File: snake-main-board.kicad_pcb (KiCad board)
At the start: 2 copper layers, 2 parts

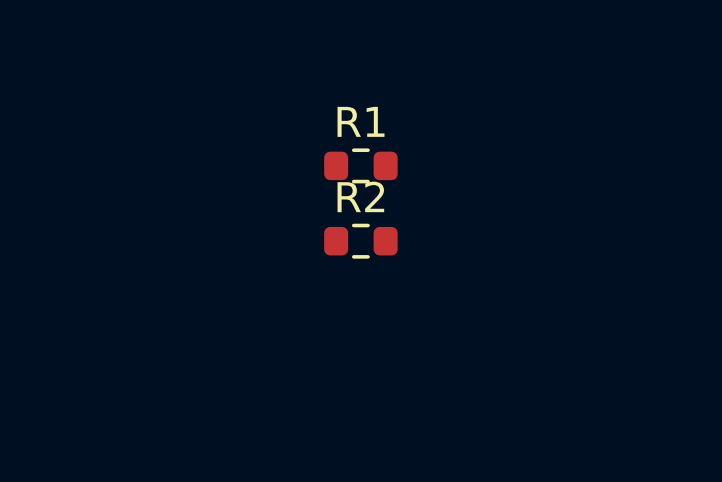
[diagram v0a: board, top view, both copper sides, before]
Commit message: PCB: board outline (20x12 mm), R2 placed 5 mm below R1, two 0.25 mm tracks matching the schematic nets (pcbnew; DRC 0 errors, 0 unconnected, 0 parity issues)
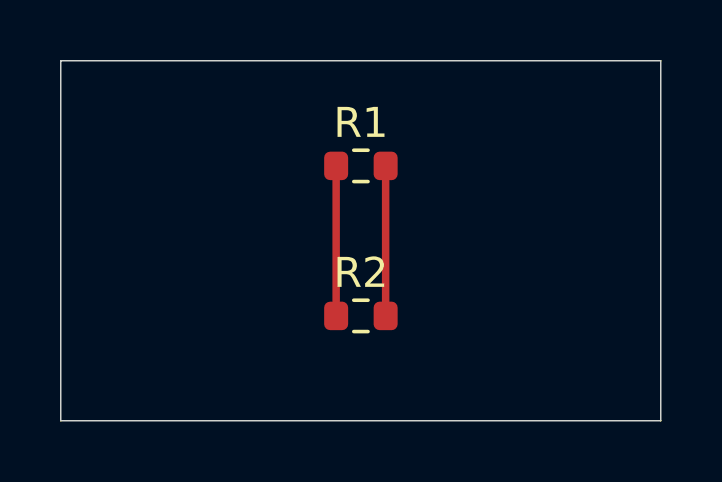
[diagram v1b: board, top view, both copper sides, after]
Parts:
- moved R2 2.49 mm to (129.5, 97.3)
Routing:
- net Net-(R1-Pad2): track 0.00 -> 5.00 mm
- net Net-(R1-Pad1): track 0.00 -> 5.00 mm
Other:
- board outline added: 20 x 12 mm
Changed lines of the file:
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@@
 	(footprint "Resistor_SMD:R_0603_1608Metric"
 		(layer "F.Cu")
-		(at 129.505 94.765)
+		(at 129.505 97.255)
 		(descr "Resistor SMD 0603 (1608 Metric), square (rectangular) end terminal, IPC-7351 nominal, (Body size source: IPC-SM-782 page 72, https://www.pcb-3d.com/wordpress/wp-content/uploads/ipc-sm-782a_amendment_1_and_2.pdf)")
 		(tags "resistor")
@@
 		)
 	)
+	(gr_rect
+		(start 119.5 88.75)
+		(end 139.5 100.75)
+		(stroke
+			(width 0.05)
+			(type default)
+		)
+		(fill no)
+		(layer "Edge.Cuts")
+	)
+	(segment
+		(start 128.68 92.255)
+		(end 128.68 97.255)
+		(width 0.25)
+		(layer "F.Cu")
+		(net "Net-(R1-Pad1)")
+	)
+	(segment
+		(start 130.33 92.255)
+		(end 130.33 97.255)
+		(width 0.25)
+		(layer "F.Cu")
+		(net "Net-(R1-Pad2)")
+	)
 	(embedded_fonts no)
